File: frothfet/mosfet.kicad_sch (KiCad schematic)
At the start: 23 parts, among them J1 Conn_01x01, Q1 BSC010N04LS, U2 LTC7004EMSE-PBF, U3 ACS725xLCTR-20AU

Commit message: updated BOM
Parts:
- C4: Mouser C0805C102J1HACTU -> (none)
- C6: Mouser C0805C472K5RAC -> (none)
- D26: LCSC (none) -> C7502719; Mouser 771-BAS416Z -> (none)
- Q1: ALT BSC010N04LS -> (none); LCSC C501508 -> (none)
- R71: value 10 -> 10R; LCSC C95781 -> C96347
- U2: LCSC C690105 -> (none)
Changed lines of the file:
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@@
 			)
 		)
+		(property "ALT" ""
+			(at 130.81 121.92 0)
+			(effects
+				(font
+					(size 1.27 1.27)
+				)
+				(hide yes)
+			)
+		)
 		(pin "1"
 		)
@@
 			)
 		)
+		(property "ALT" ""
+			(at 40.64 76.2 0)
+			(effects
+				(font
+					(size 1.27 1.27)
+				)
+				(hide yes)
+			)
+		)
 		(pin "1"
 		)
@@
 			)
 		)
-		(property "LCSC" "C690105"
+		(property "Mouser" " 584-LTC7004EMSEPBF "
 			(at 78.74 58.42 0)
 			(effects
@@
 			)
 		)
-		(property "Mouser" " 584-LTC7004EMSEPBF "
+		(property "ALT" ""
 			(at 78.74 58.42 0)
 			(effects
@@
 			)
 		)
+		(property "ALT" ""
+			(at 71.12 80.01 0)
+			(effects
+				(font
+					(size 1.27 1.27)
+				)
+				(hide yes)
+			)
+		)
 		(pin "1"
 		)
@@
 			)
 		)
+		(property "ALT" ""
+			(at 180.34 62.23 0)
+			(effects
+				(font
+					(size 1.27 1.27)
+				)
+				(hide yes)
+			)
+		)
 		(pin "1"
 		)
@@
 			)
 		)
-		(property "Value" "10"
+		(property "Value" "10R"
 			(at 134.62 73.6599 0)
 			(effects
@@
 			)
 		)
-		(property "LCSC" "C95781"
+		(property "LCSC" "C96347"
+			(at 132.08 72.39 0)
+			(effects
+				(font
+					(size 1.27 1.27)
+				)
+				(hide yes)
+			)
+		)
+		(property "ALT" ""
 			(at 132.08 72.39 0)
 			(effects
@@
 			)
 		)
+		(property "ALT" ""
+			(at 172.72 97.79 0)
+			(effects
+				(font
+					(size 1.27 1.27)
+				)
+				(hide yes)
+			)
+		)
 		(pin "1"
 		)
@@
 			)
 		)
+		(property "ALT" ""
+			(at 62.23 76.2 0)
+			(effects
+				(font
+					(size 1.27 1.27)
+				)
+				(hide yes)
+			)
+		)
 		(pin "1"
 		)
@@
 			)
 		)
+		(property "ALT" ""
+			(at 62.23 68.58 0)
+			(effects
+				(font
+					(size 1.27 1.27)
+				)
+				(hide yes)
+			)
+		)
 		(pin "1"
 		)
@@
 			)
 		)
-		(property "Mouser" " 771-BAS416Z "
+		(property "Mouser" ""
+			(at 99.06 45.72 0)
+			(effects
+				(font
+					(size 1.27 1.27)
+				)
+				(hide yes)
+			)
+		)
+		(property "LCSC" "C7502719"
+			(at 99.06 45.72 0)
+			(effects
+				(font
+					(size 1.27 1.27)
+				)
+				(hide yes)
+			)
+		)
+		(property "ALT" ""
 			(at 99.06 45.72 0)
 			(effects
@@
 			)
 		)
-		(property "Mouser" "C0805C472K5RAC"
+		(property "Mouser" ""
 			(at 176.53 114.3 0)
 			(effects
@@
 			)
 		)
+		(property "ALT" ""
+			(at 176.53 114.3 0)
+			(effects
+				(font
+					(size 1.27 1.27)
+				)
+				(hide yes)
+			)
+		)
 		(pin "1"
 		)
@@
 			)
 		)
+		(property "ALT" ""
+			(at 171.45 107.95 0)
+			(effects
+				(font
+					(size 1.27 1.27)
+				)
+				(hide yes)
+			)
+		)
 		(pin "1"
 		)
@@
 			)
 		)
+		(property "ALT" ""
+			(at 156.21 107.95 0)
+			(effects
+				(font
+					(size 1.27 1.27)
+				)
+				(hide yes)
+			)
+		)
 		(pin "1"
 		)
@@
 			)
 		)
+		(property "ALT" ""
+			(at 125.73 55.88 0)
+			(effects
+				(font
+					(size 1.27 1.27)
+				)
+				(hide yes)
+			)
+		)
 		(pin "1"
 		)
@@
 			)
 		)
-		(property "Mouser" "C0805C102J1HACTU"
+		(property "Mouser" ""
 			(at 167.64 114.3 0)
 			(effects
@@
 			)
 		)
+		(property "ALT" ""
+			(at 167.64 114.3 0)
+			(effects
+				(font
+					(size 1.27 1.27)
+				)
+				(hide yes)
+			)
+		)
 		(pin "1"
 		)
@@
 			)
 		)
+		(property "ALT" ""
+			(at 132.08 66.04 0)
+			(effects
+				(font
+					(size 1.27 1.27)
+				)
+				(hide yes)
+			)
+		)
 		(pin "1"
 		)
@@
 			)
 		)
+		(property "ALT" ""
+			(at 120.65 71.12 0)
+			(effects
+				(font
+					(size 1.27 1.27)
+				)
+				(hide yes)
+			)
+		)
 		(pin "1"
 		)
@@
 			)
 		)
+		(property "ALT" ""
+			(at 125.73 60.96 0)
+			(effects
+				(font
+					(size 1.27 1.27)
+				)
+				(hide yes)
+			)
+		)
 		(pin "1"
 		)
@@
 			)
 		)
-		(property "ALT" "BSC010N04LS"
-			(at 143.51 58.42 0)
-			(effects
-				(font
-					(size 1.27 1.27)
-				)
-				(hide yes)
-			)
-		)
-		(property "LCSC" "C501508"
+		(property "Mouser" " 726-BSC010N04LS "
 			(at 143.51 58.42 0)
 			(effects
@@
 			)
 		)
-		(property "Mouser" " 726-BSC010N04LS "
+		(property "ALT" ""
 			(at 143.51 58.42 0)
 			(effects
@@
 			)
 		)
+		(property "ALT" ""
+			(at 25.4 76.2 0)
+			(effects
+				(font
+					(size 1.27 1.27)
+				)
+				(hide yes)
+			)
+		)
 		(pin "1"
 		)
@@
 			)
 		)
+		(property "ALT" ""
+			(at 146.05 143.51 0)
+			(effects
+				(font
+					(size 1.27 1.27)
+				)
+				(hide yes)
+			)
+		)
 		(pin "1"
 		)
@@
 			)
 		)
+		(property "ALT" ""
+			(at 130.81 134.62 0)
+			(effects
+				(font
+					(size 1.27 1.27)
+				)
+				(hide yes)
+			)
+		)
 		(pin "1"
 		)
@@
 			(at 168.91 138.43 0)
 			(effects
+				(font
+					(size 1.27 1.27)
+				)
+				(hide yes)
+			)
+		)
+		(property "ALT" ""
+			(at 168.91 138.43 0)
+			(effects

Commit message: wrong led pn
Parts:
- D1: LCSC C125094 -> C98224
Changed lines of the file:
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@@
 			)
 		)
-		(property "LCSC" "C125094"
+		(property "LCSC" "C98224"
 			(at 62.23 76.2 0)
 			(effects

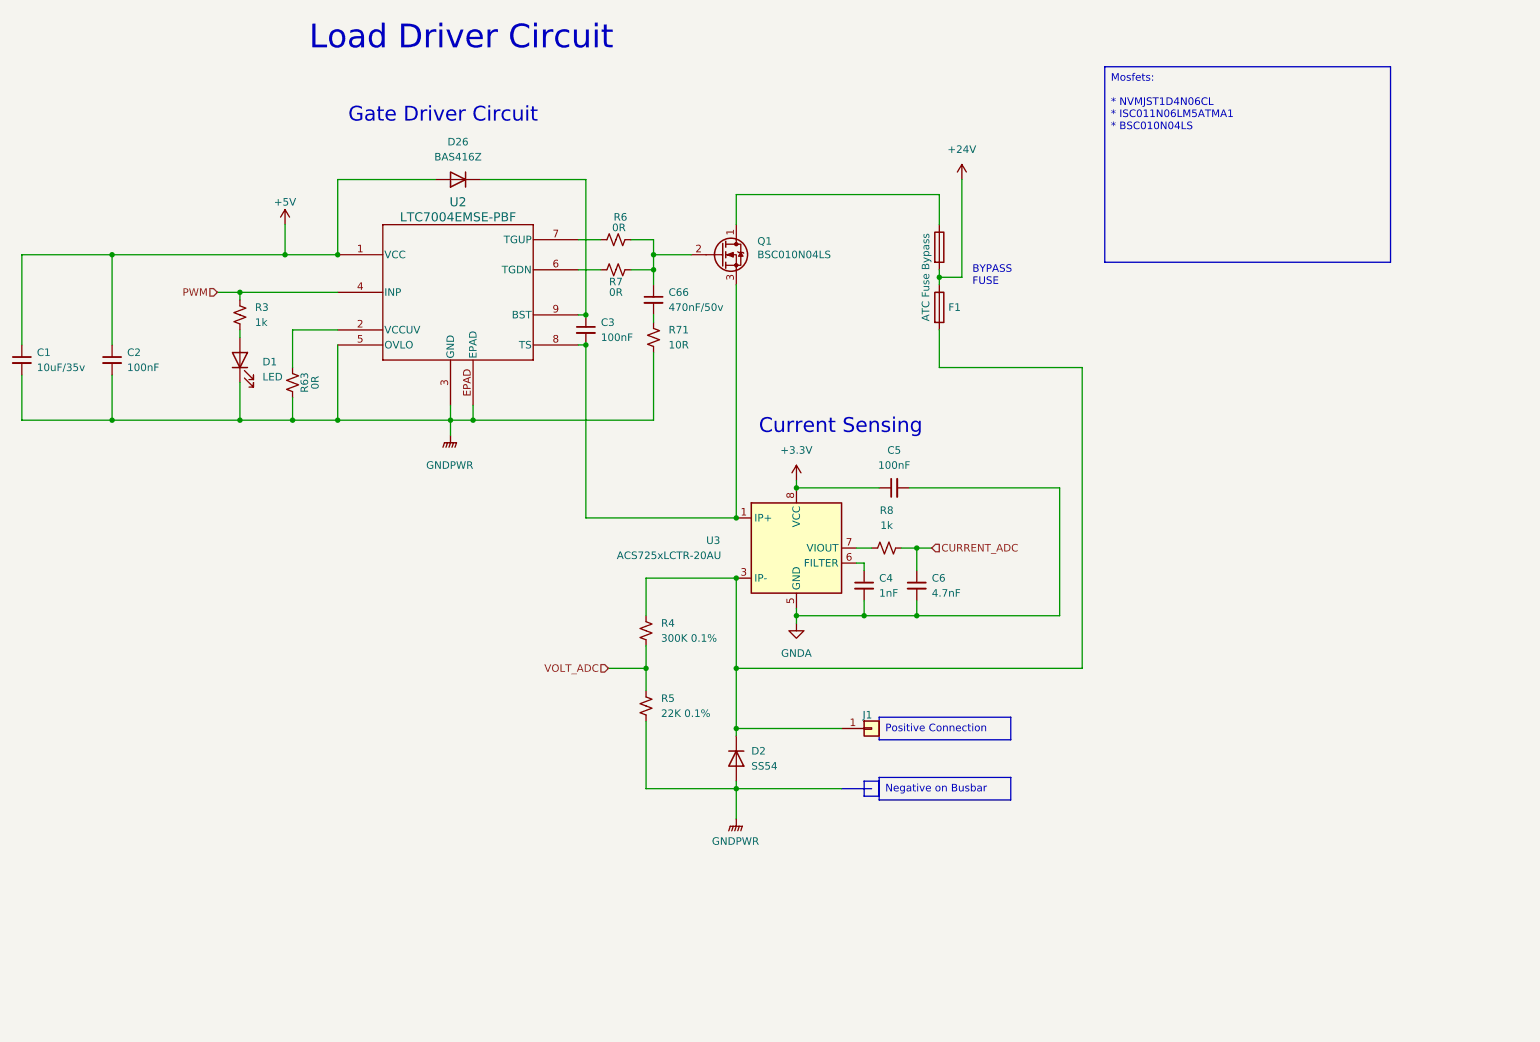
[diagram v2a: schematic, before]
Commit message: updated dnp, updatd channel voltage divider, added discharge mosfet circuit
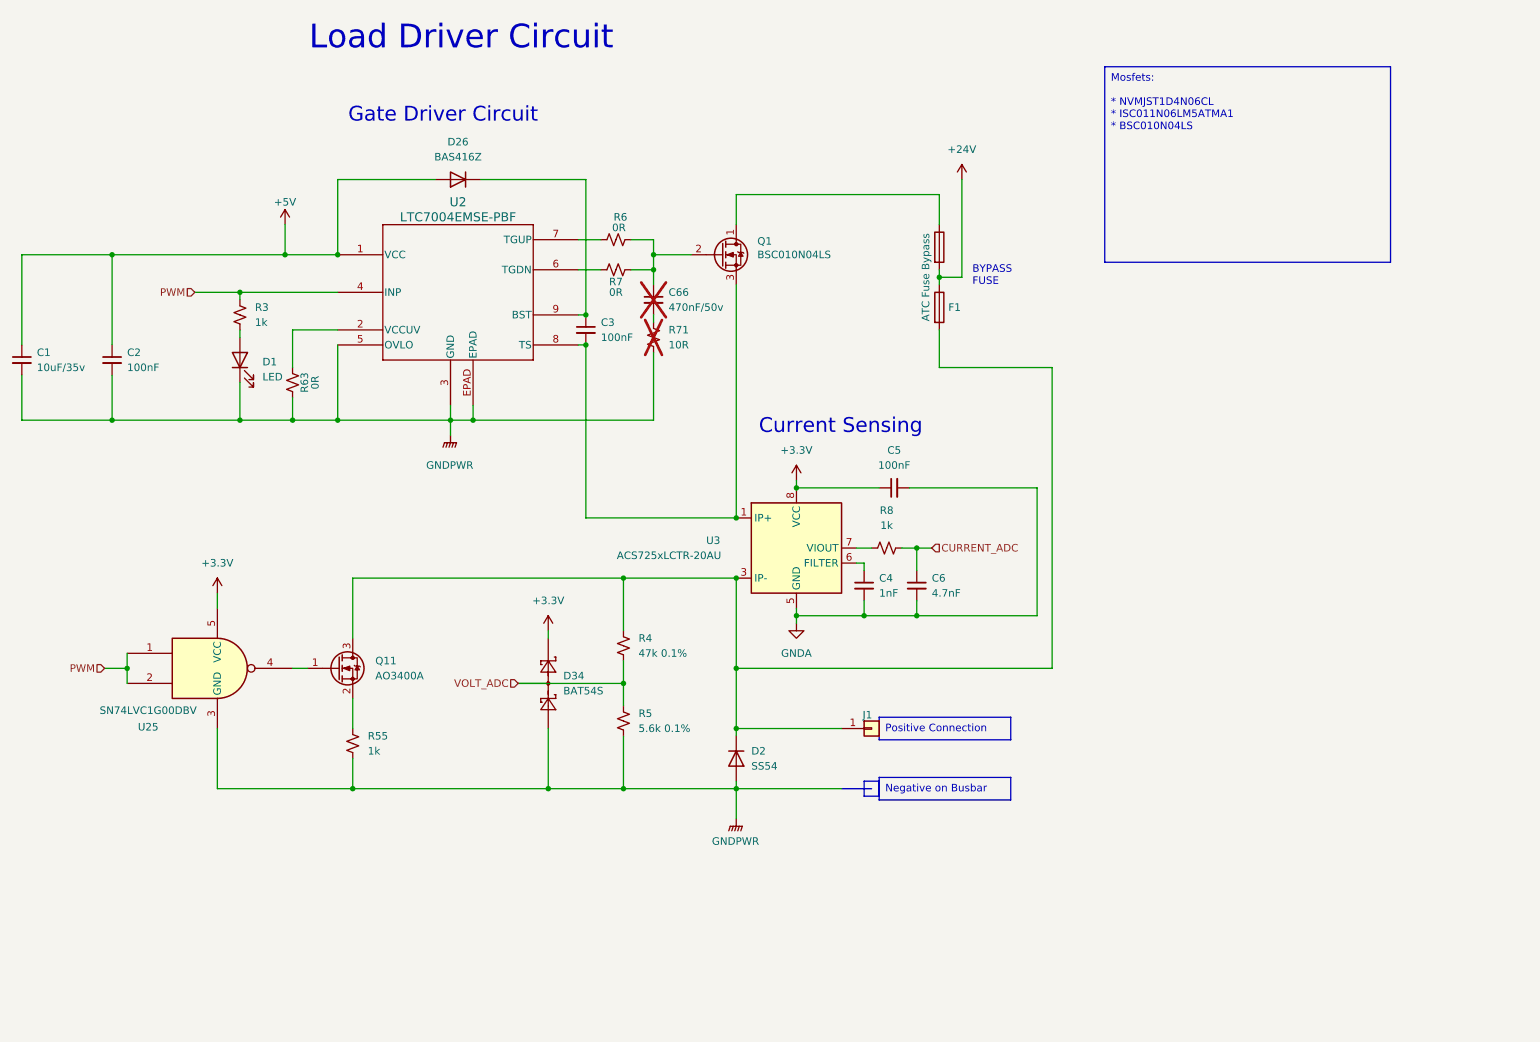
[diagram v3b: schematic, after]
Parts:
- added D34: BAT54S, Package_TO_SOT_SMD:SOT-23, symbol Diode:BAT54S
- added Q11: AO3400A, Package_TO_SOT_SMD:SOT-23, symbol Transistor_FET:AO3400A
- added R55: 1k, Resistor_SMD:R_0805_2012Metric_Pad1.20x1.40mm_HandSolder, symbol Device:R_Small_US
- added U25: SN74LVC1G00DBV, Package_TO_SOT_SMD:SOT-23-5, symbol 74xGxx:SN74LVC1G00DBV
- C66, R71: now not fitted
- R4: value 300K 0.1% -> 47k 0.1%; LCSC C865386 -> (none)
- R5: value 22K 0.1% -> 5.6k 0.1%; LCSC C865312 -> (none)
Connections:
- net +3.3V: now also D34.2 (K), U25.5 (VCC)
- net GNDPWR: now also D34.1 (A), R55.1, U25.3 (GND)
- net PWM: now also U25.1, U25.2
- net VOLT_ADC: now also D34.3 (COM)
- net at D2.1 (K), F1.3, J1.1 (Pin_1)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: now also Q11.3 (D)
- new net: Q11.1 (G), U25.4
- new net: Q11.2 (S), R55.2
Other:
- moved on the sheet: R4, R5

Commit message: todo list and rev d testing
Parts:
- removed U25: SN74LVC1G00DBV, Package_TO_SOT_SMD:SOT-23-5, symbol 74xGxx:SN74LVC1G00DBV
- added U25: SN74LVC1G14DBV, Package_TO_SOT_SMD:SOT-23-5, symbol 74xGxx:SN74LVC1G14DBV
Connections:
- net +3.3V: now also U25.5 (VCC)
- net GNDPWR: now also U25.3 (GND)
- net PWM: now also U25.2
- net at Q11.1 (G): now also U25.4
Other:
- moved on the sheet: F1, Q11, R55

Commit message: updated voltage divider values
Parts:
- R4: value 47k 0.1% -> 470k 0.1%
- R5: value 5.6k 0.1% -> 57.6k 0.1%
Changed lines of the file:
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@@
 			)
 		)
-		(property "Value" "47k 0.1%"
+		(property "Value" "470k 0.1%"
 			(at 129.54 125.73 0)
 			(effects
@@
 			)
 		)
-		(property "Value" "5.6k 0.1%"
+		(property "Value" "57.6k 0.1%"
 			(at 129.54 138.43 0)
 			(effects

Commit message: updated fans and also new "dump" mosfet circuit
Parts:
- R55: value 1k -> 100R
- U25: value SN74LVC1G14DBV -> SN74AUP1G04DBVR
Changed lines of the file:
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@@
 			)
 		)
-		(property "Value" "1k"
+		(property "Value" "100R"
 			(at 85.09 142.24 0)
 			(effects
@@
 			)
 		)
-		(property "Value" "SN74LVC1G14DBV"
+		(property "Value" "SN74AUP1G04DBVR"
 			(at 62.23 120.142 0)
 			(effects
@@
 			)
 		)
-		(property "Datasheet" "https://www.ti.com/lit/ds/symlink/sn74lvc1g14.pdf"
+		(property "Datasheet" "https://www.ti.com/lit/gpn/sn74aup1g04"
 			(at 57.15 137.16 0)
 			(effects

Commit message: rev e channel changes.
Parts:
- removed D1: LED, LED_SMD:LED_0805_2012Metric_Pad1.15x1.40mm_HandSolder, symbol Device:LED
- removed R3: 1k, Resistor_SMD:R_0805_2012Metric_Pad1.20x1.40mm_HandSolder, symbol Device:R_Small_US
- removed R71: 10R, Resistor_SMD:R_0805_2012Metric_Pad1.20x1.40mm_HandSolder, symbol Device:R_Small_US
- added D1: WS2812B-2020, LED_SMD:LED_WS2812B-2020_PLCC4_2.0x2.0mm, symbol LED:WS2812B-2020
- C3: value 100nF -> 220nF
- C66: value 470nF/50v -> 100nF; LCSC C106843 -> C49678; now fitted
- R6: value 0R -> 10R
- R63: value 0R -> 150K
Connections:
- net +5V: now also C66.2, D1.4 (VDD)
- net GNDPWR: now also C66.1, D1.2 (VSS)
- net at Q1.2 (G), R6.1, R7.1: no longer C66.1
- new net LED_DIN: D1.3 (DIN)
- new net LED_DOUT: D1.1 (DOUT)
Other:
- moved on the sheet: C1, C2

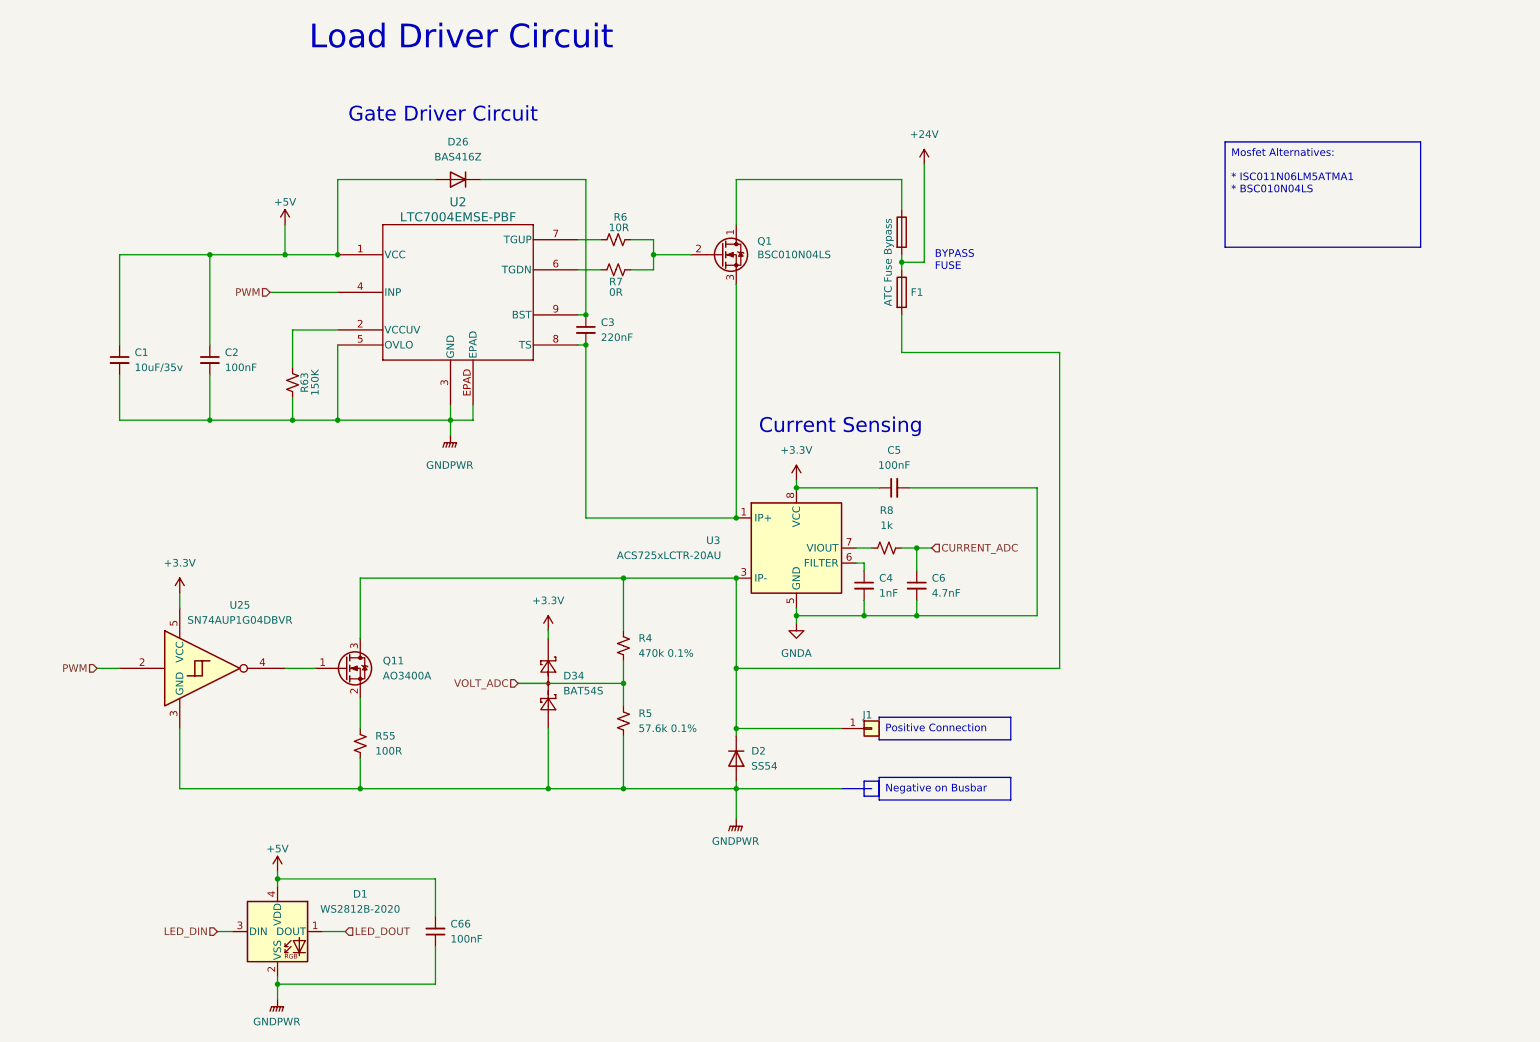
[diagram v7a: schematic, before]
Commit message: updated the dummy load schematic.
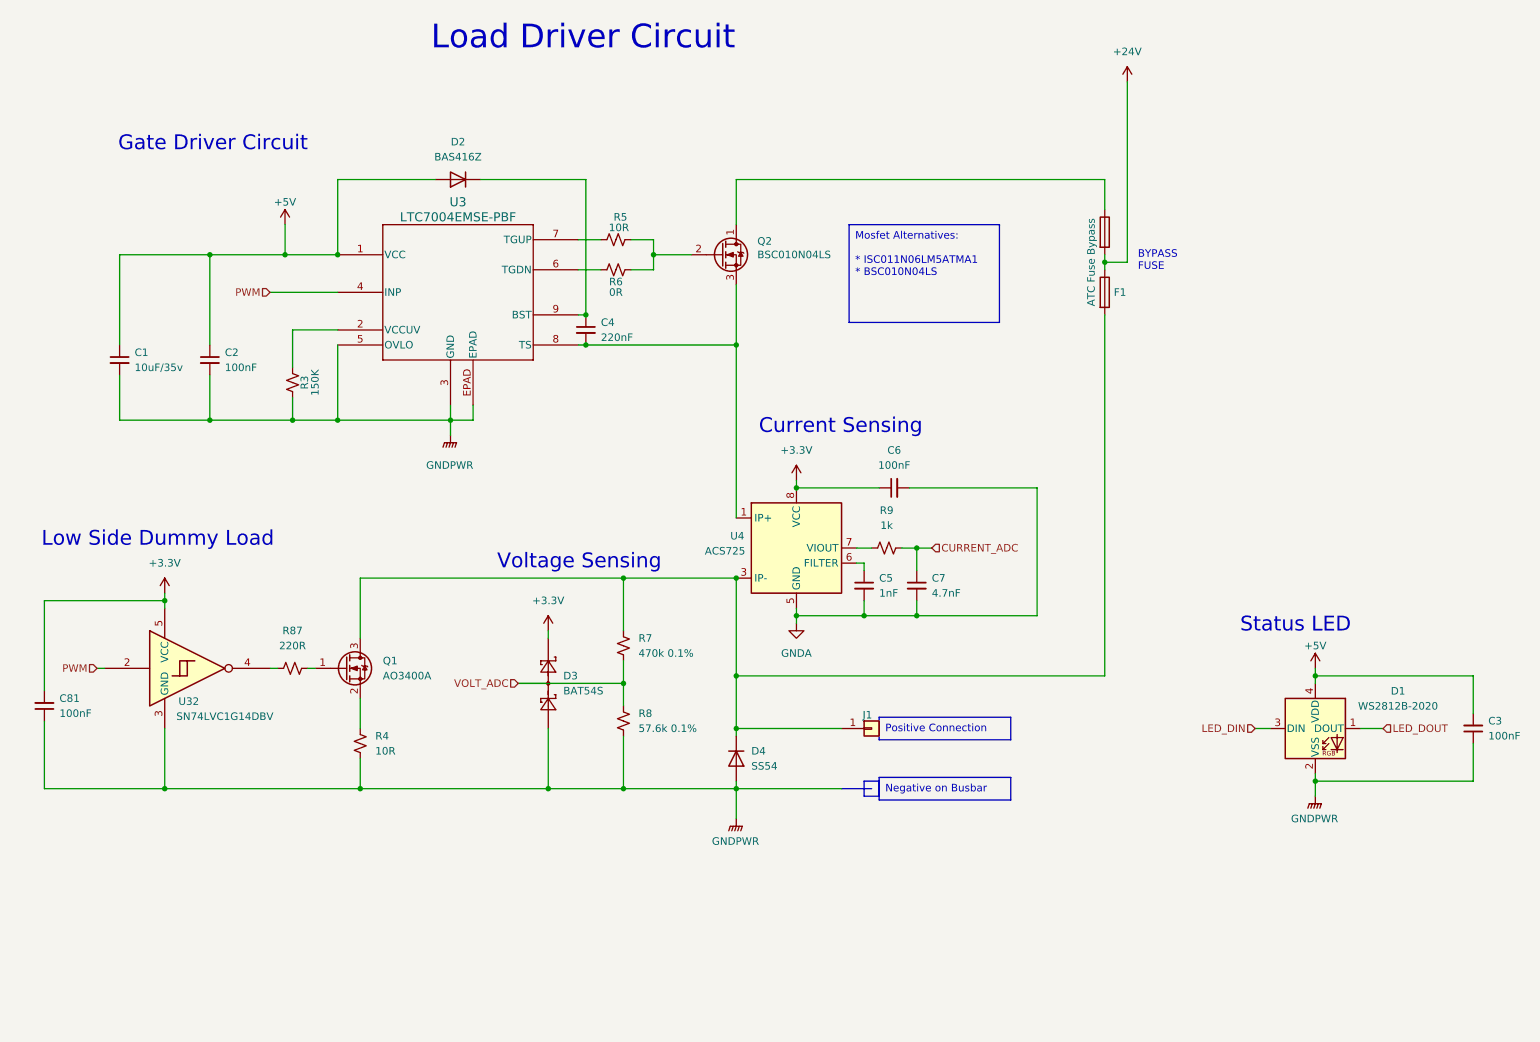
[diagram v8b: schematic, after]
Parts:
- removed U25: SN74AUP1G04DBVR, Package_TO_SOT_SMD:SOT-23-5, symbol 74xGxx:SN74LVC1G14DBV
- added C81: 100nF, Capacitor_SMD:C_0805_2012Metric_Pad1.18x1.45mm_HandSolder, symbol Device:C_Small
- added R87: 220R, Resistor_SMD:R_0805_2012Metric_Pad1.20x1.40mm_HandSolder, symbol Device:R_Small_US
- added U32: SN74LVC1G14DBV, Package_TO_SOT_SMD:SOT-23-5, symbol 74xGxx:SN74LVC1G14DBV
- R4: renamed from R55; value 100R -> 10R
- U4: renamed from U3; value ACS725xLCTR-20AU -> ACS725
- renumbered C66 to C3, C3 to C4, C4 to C5, C5 to C6, C6 to C7, D26 to D2, D34 to D3, D2 to D4, Q11 to Q1, Q1 to Q2, R63 to R3, R6 to R5, R7 to R6, R4 to R7, R5 to R8, R8 to R9, U2 to U3
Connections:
- net +3.3V: now also C81.2, U32.5 (VCC)
- net GNDPWR: now also C81.1, U32.3 (GND)
- net PWM: now also U32.2
- net at Q1.1 (G): now also R87.1
- new net: R87.2, U32.4
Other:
- note added: "Low Side Dummy Load"
- note added: "Status LED"
- note added: "Voltage Sensing"
- moved on the sheet: C3, D1, F1
